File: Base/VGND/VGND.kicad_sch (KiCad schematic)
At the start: 35 parts, among them J1 Ground, J2 Barrel_Jack_Switch, J3 Conn_01x03_Pin, J4 Conn_01x03_Pin, J5 AudioJack2_Ground, J6 AudioJack2_Ground, Q1 40V, U1 TLE2426xD, U2 OPA1656

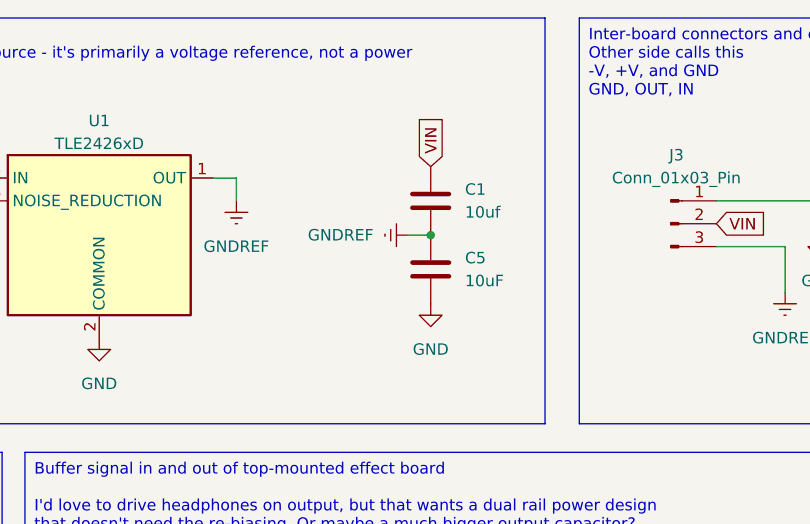
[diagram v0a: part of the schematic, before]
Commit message: Oops, fix the 4.5V ref voltage - remove the coupling capacitors
The bypass caps came from the "real ground" circuits that had dual
voltage rails, but they are very wrong for the 4.5V ground generated by
the TLE2426.

There's even a big comment saying that it's a voltage reference, not a
power supply, but I didn't think it through.  Having the caps to the
real voltage rails just makes the 2426 oscillate, so don't do it.

The good news? The boards work, just make sure to not populate the caps.

Signed-off-by: Linus Torvalds <torvalds@linux-foundation.org>
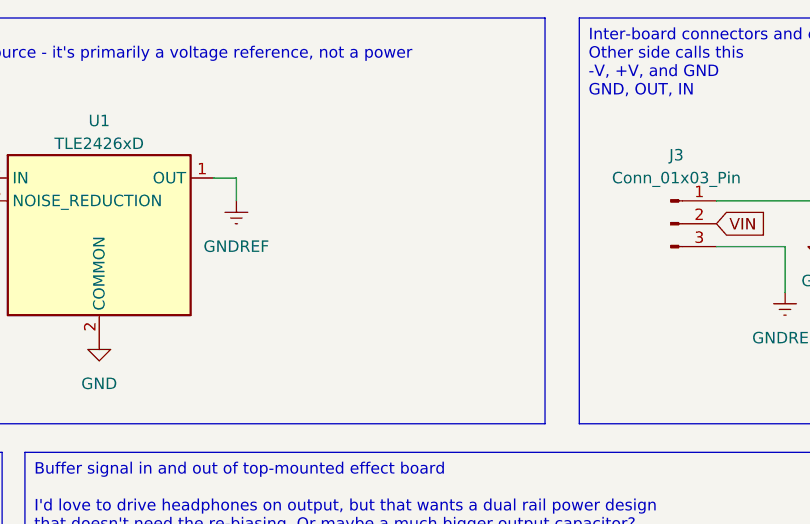
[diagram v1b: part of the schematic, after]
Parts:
- removed C1: 10uf, Capacitor_SMD:C_1206_3216Metric_Pad1.33x1.80mm_HandSolder, symbol Device:C
- removed C5: 10uF, Capacitor_SMD:C_1206_3216Metric_Pad1.33x1.80mm_HandSolder, symbol Device:C

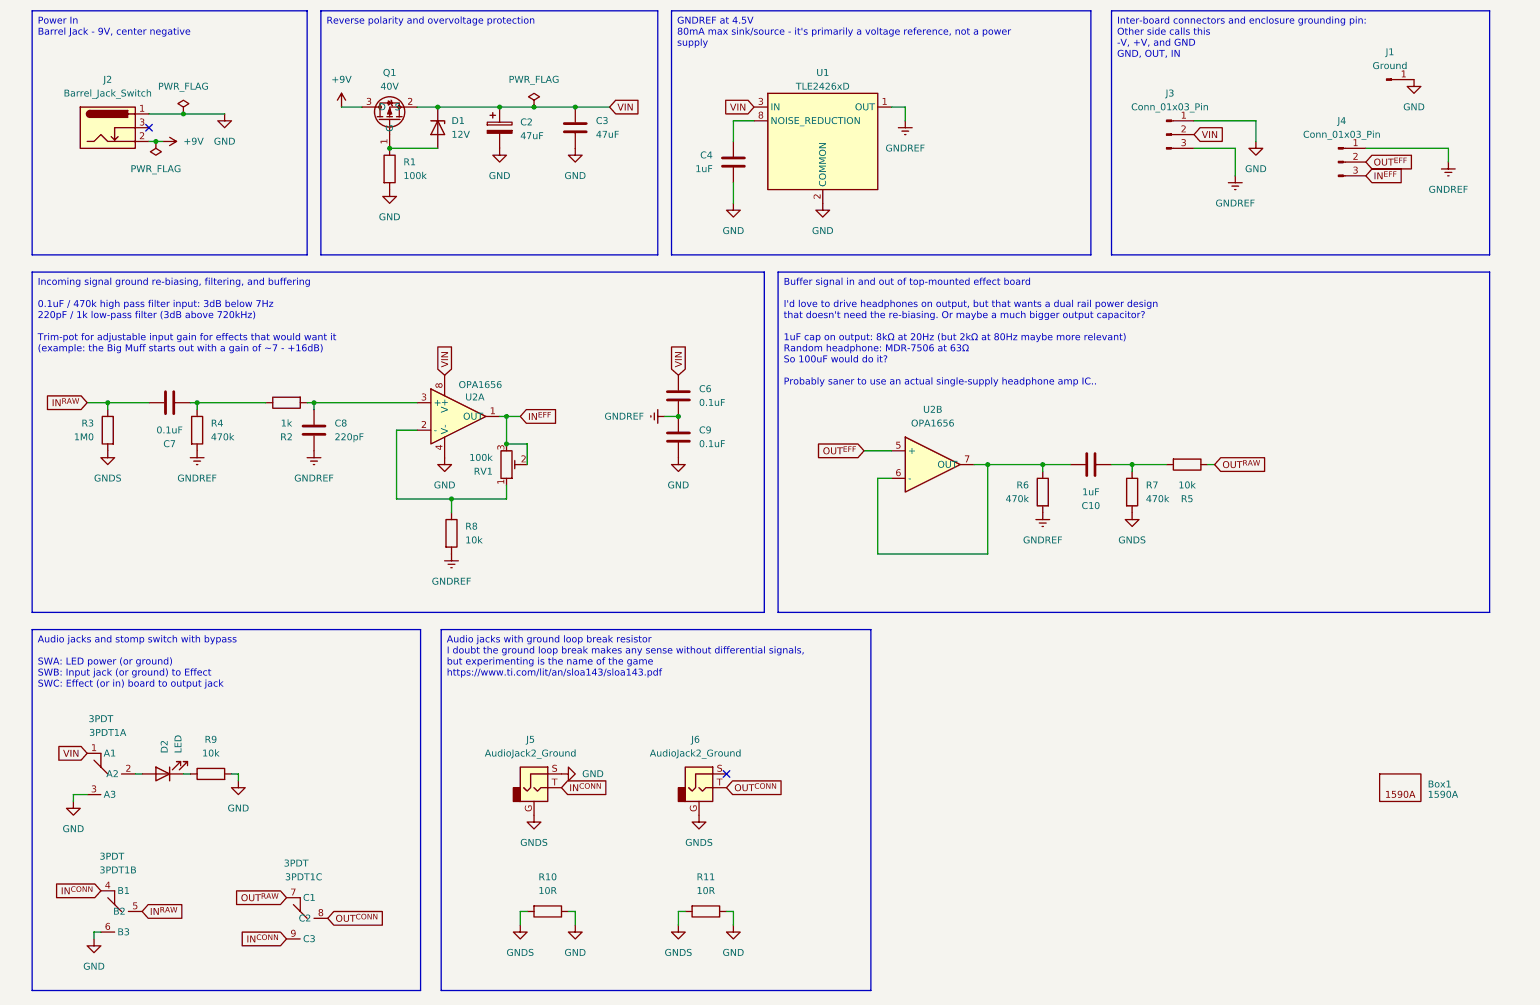
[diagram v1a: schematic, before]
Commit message: Stop trying to pretend that the 4.5V reference voltage is ground
Yes, it was a real ground in the earlier dual rail supply designs, but
in Gen2 that's no longer the case, and the pretense caused issues with
me adding bypass capacitors to that reference voltage rail.

So this just renames it as 'GNDREF' everywhere.  Maybe I should have
called it 'VREF'?

The real ground is still called '-V' in the effects, I'll change that
later too, but let's do this in individual steps.

This also removes the remaining bypass caps to GNDREF, and makes the
ground pours be actual ground.

I also need to come up with something sane for the Rectifier board
potentiometers.

Right now they are bogus random stuff where I am using the pots as
trim-pots for testing, but they don't actually make *sense* (ie the
"Volume" pot isn't actually sane, it ends up being another voltage
divider with the resistors in the low-pass filter trim pot etc).

Signed-off-by: Linus Torvalds <torvalds@linux-foundation.org>
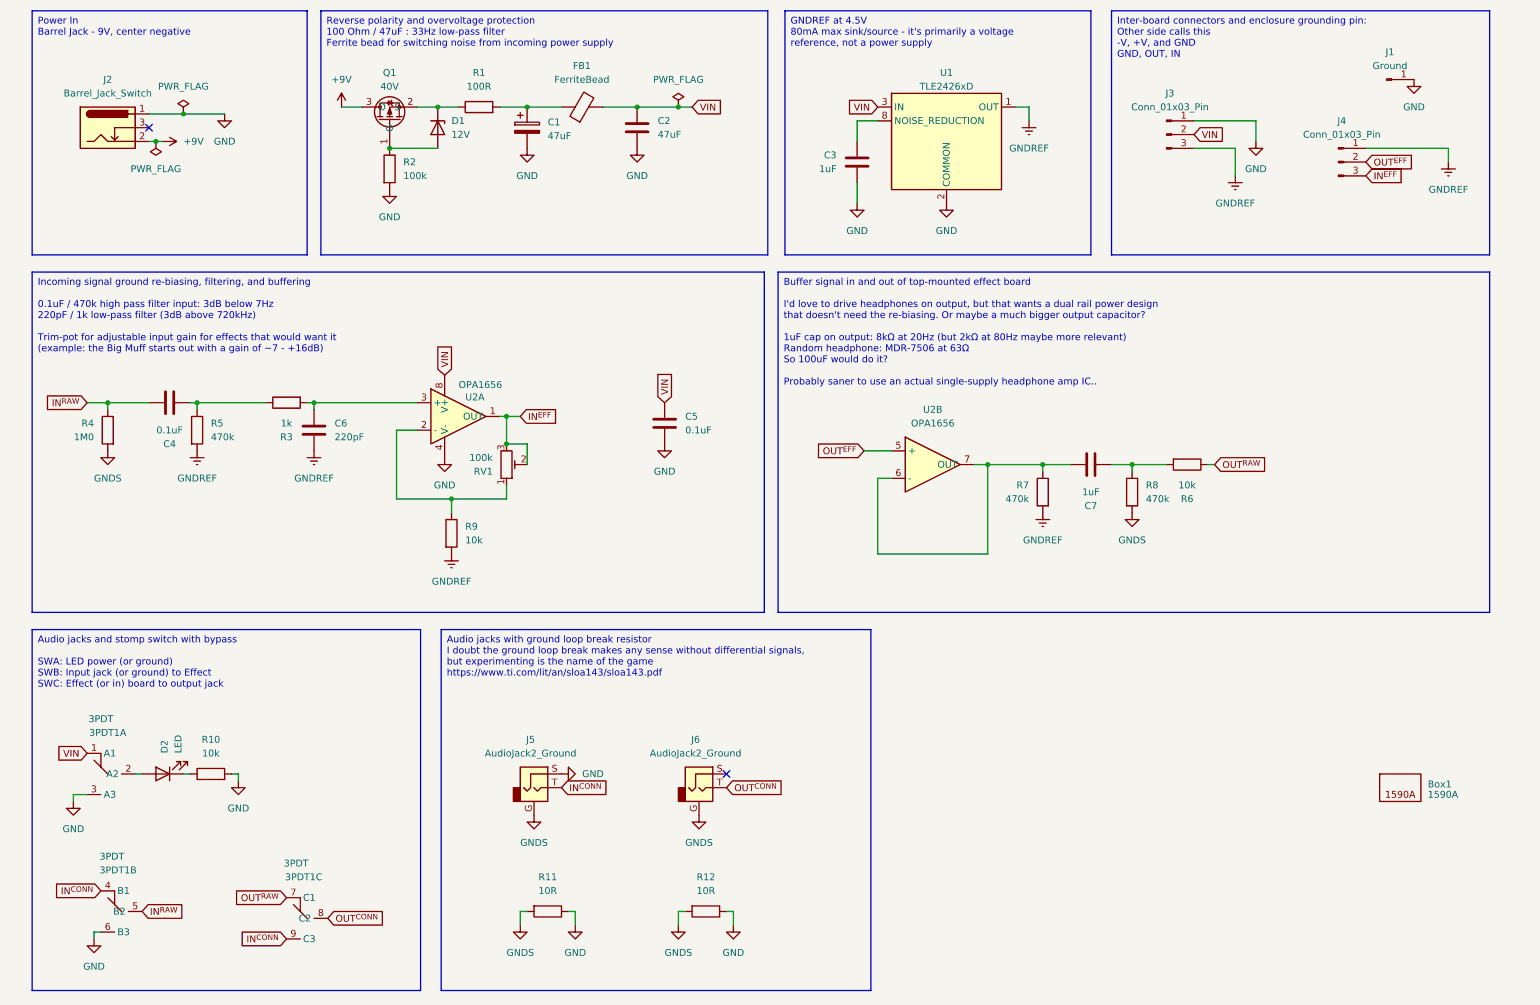
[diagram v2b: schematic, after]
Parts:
- removed C9: 0.1uF, Mylib:C_0704_1810Metric, symbol Device:C
- added FB1: FerriteBead, Inductor_SMD:L_1206_3216Metric_Pad1.22x1.90mm_HandSolder, symbol Device:FerriteBead
- added R1: 100R, Resistor_SMD:R_0805_2012Metric_Pad1.20x1.40mm_HandSolder, symbol Device:R
- renumbered C2 to C1, C3 to C2, C4 to C3, C7 to C4, C6 to C5, C8 to C6, C10 to C7, R9 to R10, R10 to R11, R11 to R12, R1 to R2, R2 to R3, R3 to R4, R4 to R5, R5 to R6, R6 to R7, R7 to R8, R8 to R9
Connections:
- net GND: now also C5.2
- net GNDREF: no longer C5.2
- net VIN: now also FB1.2; no longer C1.1, D1.1 (K), Q1.2 (S)
- new net: C1.1, FB1.1, R1.2
- new net: D1.1 (K), Q1.2 (S), R1.1
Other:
- moved on the sheet: C1, C2, C3, C5, U1

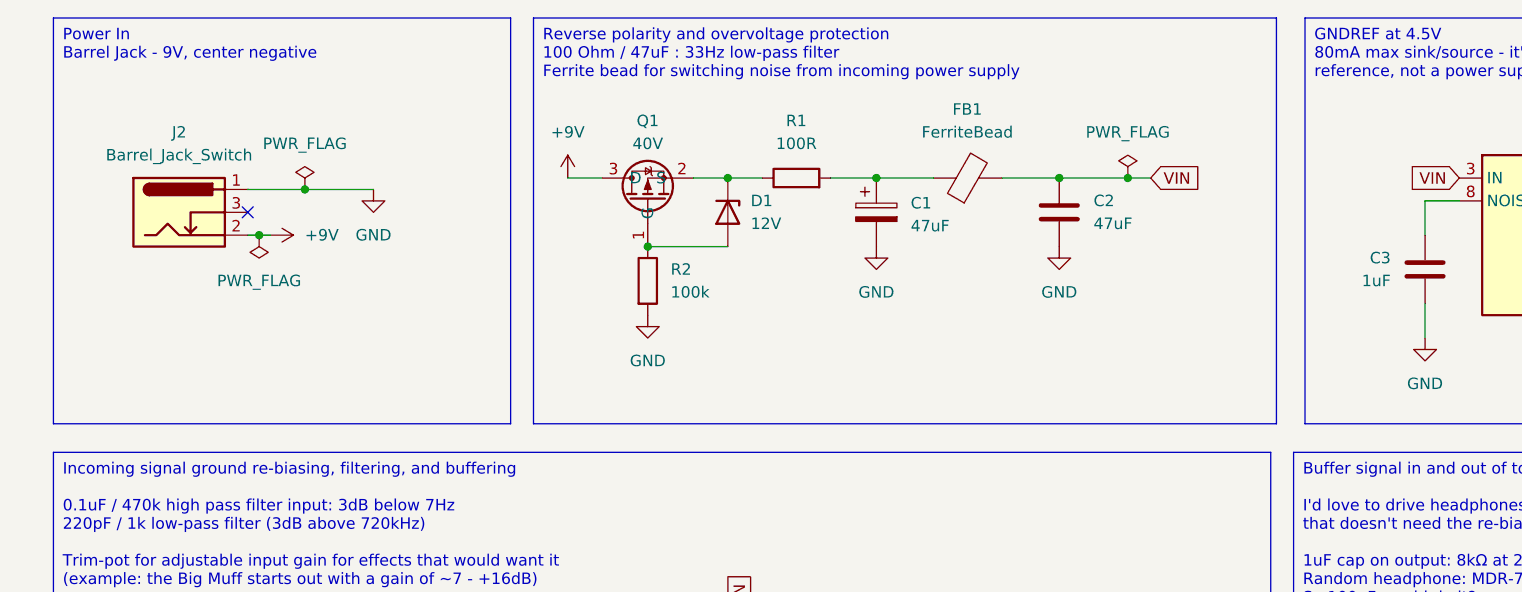
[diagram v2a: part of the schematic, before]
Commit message: Trivial updates to the VGND board
This is mainly just some added experimental noise suppression, with an
optional ferrite bead on the power ground connection too.

None of this should matter - or necessarily even be a good idea - for a
good pedal power supply with clean power, but this is mostly just a
reaction to a not-so-good no-name power supply that was very noisy
indeed.  It's just been pending while I was busy with the kernel merge
window.

I threw that power supply out in disgust, which was a mistake.  I should
have kept it for testing this.

But even if the ferrite beads don't end up working or making any sense,
it's easy enough to just bridge them.  It's hard to try to add them to a
board that doesn't have the space for them.

Signed-off-by: Linus Torvalds <torvalds@linux-foundation.org>
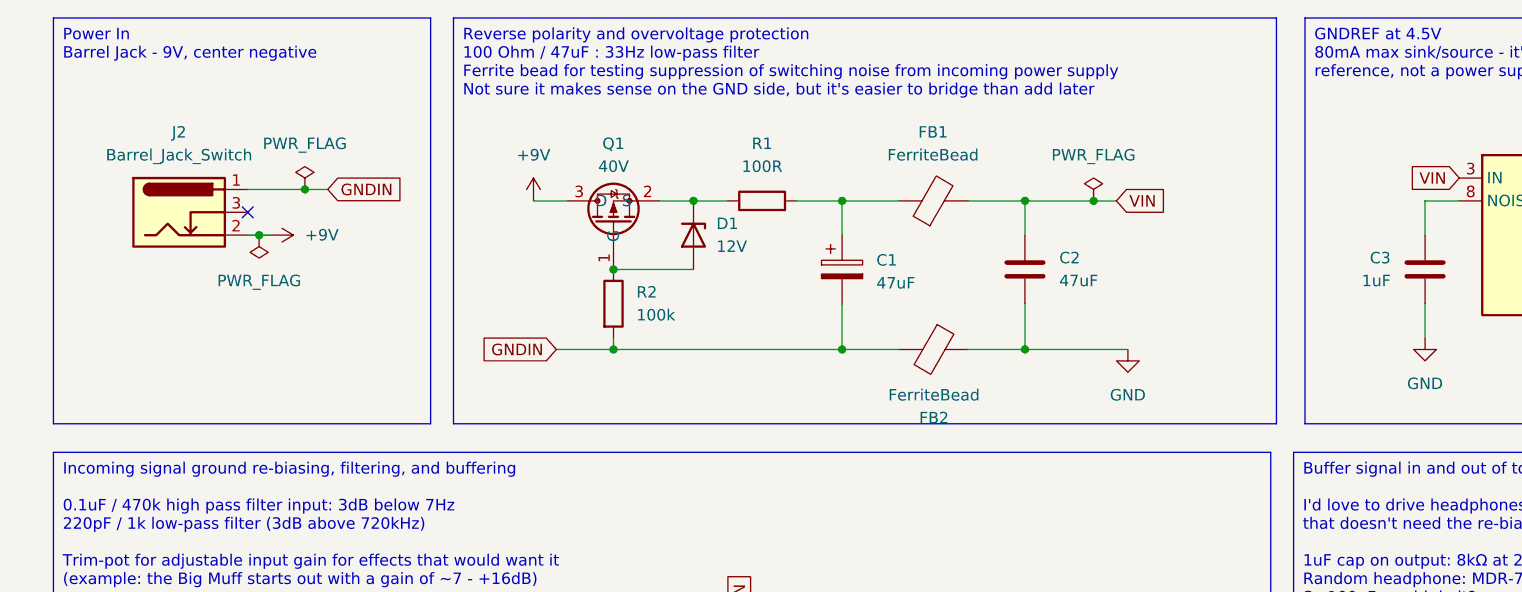
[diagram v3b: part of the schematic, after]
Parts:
- added FB2: FerriteBead, Inductor_SMD:L_1206_3216Metric_Pad1.22x1.90mm_HandSolder, symbol Device:FerriteBead
- Q1: footprint Package_TO_SOT_SMD:SOT-23-3 -> SOT-23-3
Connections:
- net GND: now also FB2.1; no longer C1.2, J2.1, R2.2
- new net GNDIN: C1.2, FB2.2, J2.1, R2.2
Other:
- moved on the sheet: C1, C2, D1, FB1, Q1, R1, R2
